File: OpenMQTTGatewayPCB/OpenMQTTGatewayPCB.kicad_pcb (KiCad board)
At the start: 2 copper layers, 91.4 x 91.4 mm, 33 parts, among them J2 Conn_01x02_Male, J3 Conn_Coaxial, J4 Conn_Coaxial, Q1 BCP56, U1 nodemcu_v0.9, U2 DHT11, U3 TSOP21xx, U4 SRX882, U5 STX882, U6 HM-10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

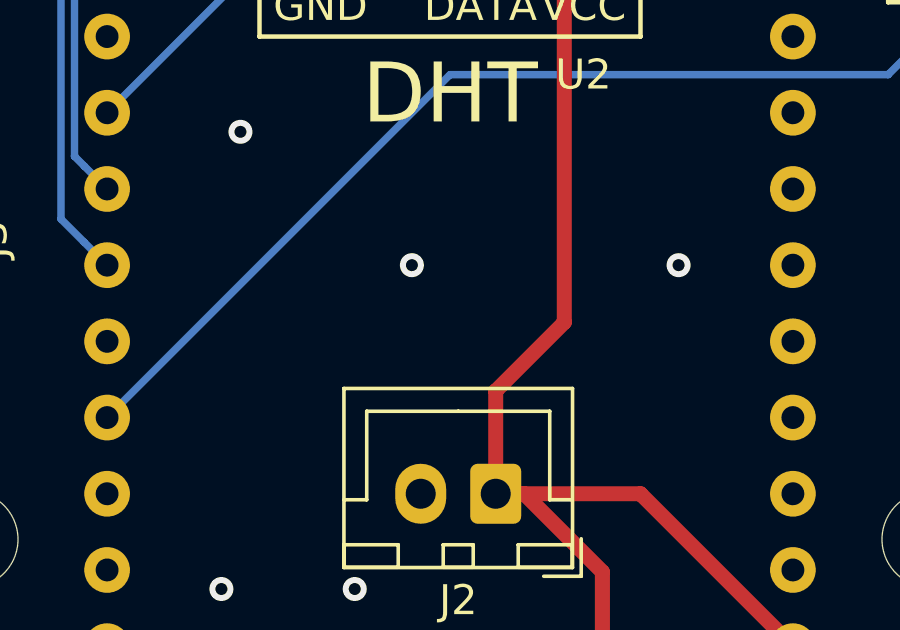
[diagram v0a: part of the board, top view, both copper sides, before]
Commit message: Added Silkscrean for Power input
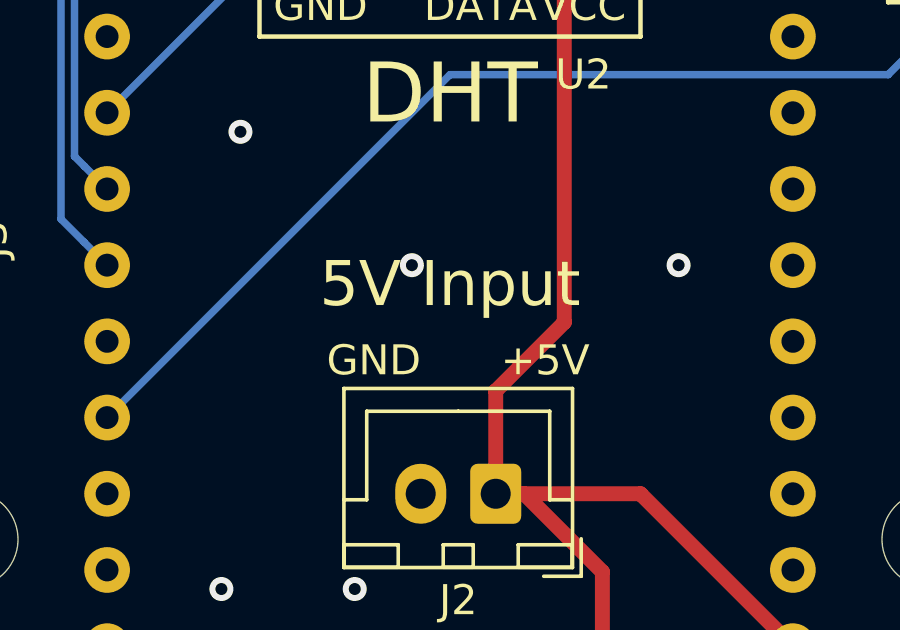
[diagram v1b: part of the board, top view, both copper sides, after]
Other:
- board text added: "+5V"
- board text added: "5V Input"
- board text added: "GND"
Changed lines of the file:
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@@
   (general
     (thickness 1.6)
-    (drawings 16)
+    (drawings 19)
     (tracks 219)
     (zones 0)
@@
   )
   (setup
-    (last_trace_width 0.5)
+    (last_trace_width 0.25)
     (user_trace_width 0.5)
     (trace_clearance 0.2)
@@
     )
   )
+  (gr_text +5V (at 99.695 99.695) (layer F.SilkS)
+    (effects (font (size 1 1) (thickness 0.15)))
+  )
+  (gr_text "GND\n" (at 93.98 99.695) (layer F.SilkS)
+    (effects (font (size 1 1) (thickness 0.15)))
+  )
+  (gr_text "5V Input" (at 96.52 97.155) (layer F.SilkS)
+    (effects (font (size 1.5 1.5) (thickness 0.3)))
+  )
   (gr_text BT (at 96.52 36.195) (layer B.SilkS)

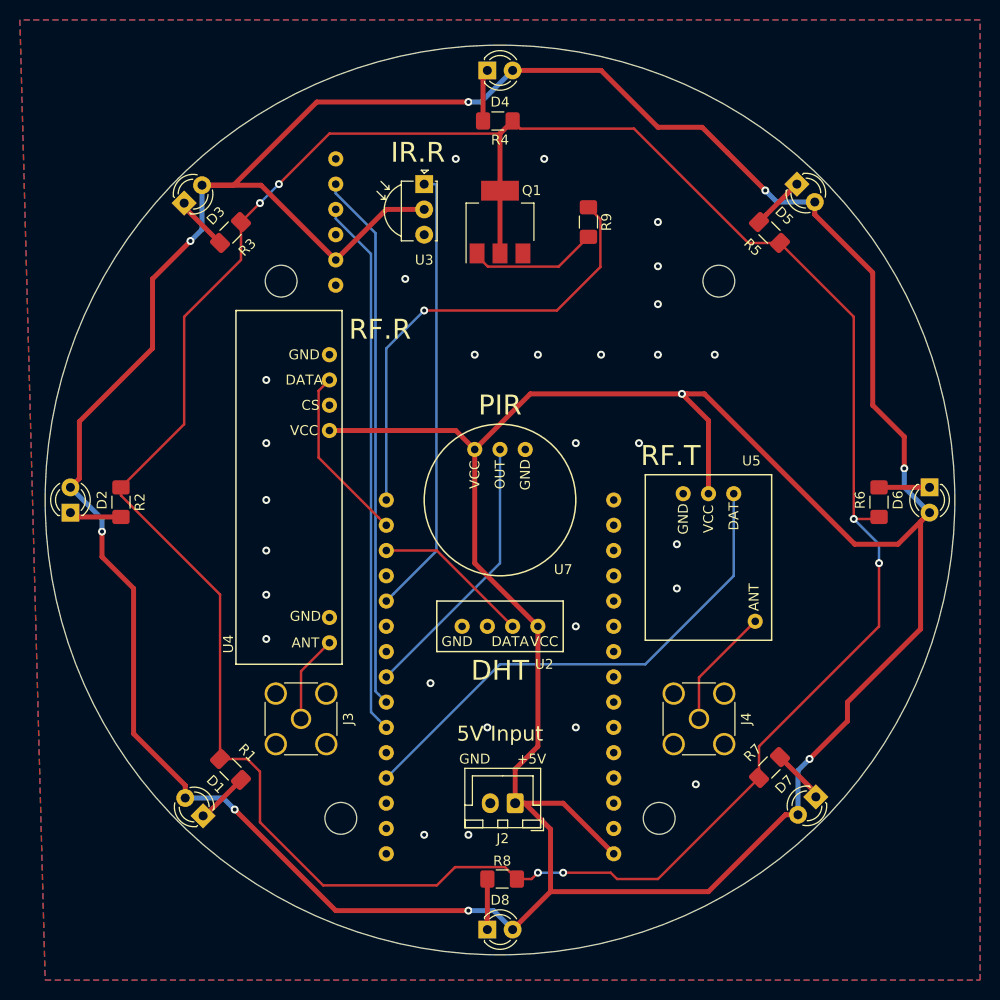
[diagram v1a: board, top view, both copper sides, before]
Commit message: Fixed all known issues of rev1
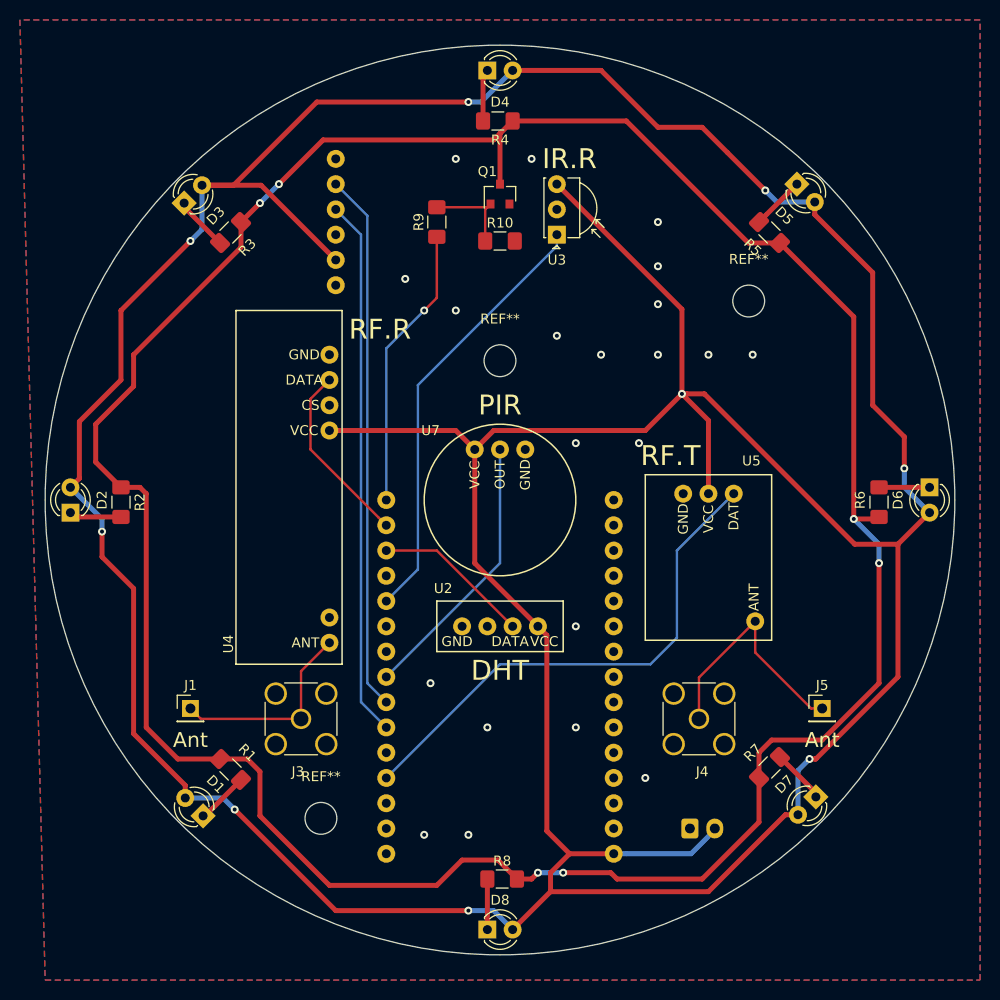
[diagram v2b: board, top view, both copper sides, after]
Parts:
- removed the REF** at (80.5, 105.7)
- removed the REF** at (112.5, 105.7)
- removed the REF** at (118.5, 51.7)
- removed the REF** at (74.5, 51.7)
- removed the REF** at (76.2, 73.7)
- added J1: Antenna Con, Connector_PinHeader_2.54mm:PinHeader_1x01_P2.54mm_Vertical, F.Cu at (65.4, 94.6)
- added J5: Antenna Con, Connector_PinHeader_2.54mm:PinHeader_1x01_P2.54mm_Vertical, F.Cu at (128.9, 94.6)
- added R10: 1K, Resistor_SMD:R_1206_3216Metric_Pad1.42x1.75mm_HandSolder, F.Cu at (96.5, 47.6)
- added REF**: MountingHole_3.2mm_M3, MountingHole:MountingHole_3.2mm_M3, F.Cu at (121.5, 53.7)
- added REF**: MountingHole_3.2mm_M3, MountingHole:MountingHole_3.2mm_M3, F.Cu at (78.5, 105.7)
- added REF**: MountingHole_3.2mm_M3, MountingHole:MountingHole_3.2mm_M3, F.Cu at (96.5, 59.7)
- added REF**: OSHW-Logo_7.5x8mm_SilkScreen, Symbol:OSHW-Logo_7.5x8mm_SilkScreen, B.Cu at (73.0, 85.7)
- added REF**: KiCad-Logo2_8mm_SilkScreen, Symbol:KiCad-Logo2_8mm_SilkScreen, B.Cu at (73.0, 66.0)
- J2: moved to B.Cu
- Q1: value BCP56 -> AO3402; footprint Package_TO_SOT_SMD:SOT-223 -> Package_TO_SOT_SMD:SOT-23
- R1, R2, R3, R4, R5, R6, R7, R8: value 182R -> 47R
- U3: value TSOP21xx -> TSOP34S40F
- moved J2 17.7 mm to (115.6, 106.7), turned to 0 degrees
- moved R9 15.2 mm to (90.2, 45.7), turned to 90 degrees
- moved U3 14.3 mm to (102.2, 47.0), turned to 90 degrees
- moved Q1 2.81 mm to (96.5, 42.9)
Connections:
- J2 pad 1: +5V -> GND
- J2 pad 2: GND -> +5V
- Q1 pad 2: Net-(Q1-Pad2) -> GND
- Q1 pad 3: GND -> Net-(Q1-Pad3)
- R1 pad 2: Net-(Q1-Pad2) -> Net-(Q1-Pad3)
- R2 pad 2: Net-(Q1-Pad2) -> Net-(Q1-Pad3)
- R3 pad 2: Net-(Q1-Pad2) -> Net-(Q1-Pad3)
- R4 pad 2: Net-(Q1-Pad2) -> Net-(Q1-Pad3)
- R5 pad 2: Net-(Q1-Pad2) -> Net-(Q1-Pad3)
- R6 pad 2: Net-(Q1-Pad2) -> Net-(Q1-Pad3)
- R7 pad 2: Net-(Q1-Pad2) -> Net-(Q1-Pad3)
- R8 pad 2: Net-(Q1-Pad2) -> Net-(Q1-Pad3)
- U3 pad 2: +5V -> GND
- U3 pad 3: GND -> +5V
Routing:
- net Net-(Q1-Pad3): track 0.00 -> 277.1 mm, vias 0 -> 6
- net Net-(Q1-Pad2): track 272.5 -> 0.00 mm, vias 6 -> 0
- net D0: track 46.6 -> 28.6 mm
- net +5V: track 459.2 -> 473.2 mm
- net Net-(J4-Pad1): track 12.1 -> 24.3 mm
- net Net-(J1-Pad1): track 8.83 -> 20.4 mm
- net Net-(Q1-Pad1): track 13.1 -> 9.47 mm
- net D4: track 45.2 -> 43.9 mm
- net D1: track 17.9 -> 18.6 mm
- net GND: vias 28 -> 21
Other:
- board text added: "5V"
- board text added: "Ant"
- board text removed: "5V Input"

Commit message: Final touches for release
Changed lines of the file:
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@@
   )
   (setup
-    (last_trace_width 0.5)
+    (last_trace_width 0.25)
     (user_trace_width 0.5)
     (trace_clearance 0.2)
@@
     (tags "mounting hole 3.2mm no annular m3")
     (attr virtual)
-    (fp_text reference REF** (at 0 -4.2) (layer F.SilkS)
+    (fp_text reference REF** (at 0 -4.2) (layer F.SilkS) hide
       (effects (font (size 1 1) (thickness 0.15)))
     )
@@
     (tags "mounting hole 3.2mm no annular m3")
     (attr virtual)
-    (fp_text reference REF** (at 0 -4.2) (layer F.SilkS)
+    (fp_text reference REF** (at 0 -4.2) (layer F.SilkS) hide
       (effects (font (size 1 1) (thickness 0.15)))
     )
@@
     (tags "mounting hole 3.2mm no annular m3")
     (attr virtual)
-    (fp_text reference REF** (at 0 -4.2) (layer F.SilkS)
+    (fp_text reference REF** (at 0 -4.2) (layer F.SilkS) hide
       (effects (font (size 1 1) (thickness 0.15)))
     )
